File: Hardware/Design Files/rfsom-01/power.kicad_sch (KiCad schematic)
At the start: 26 parts

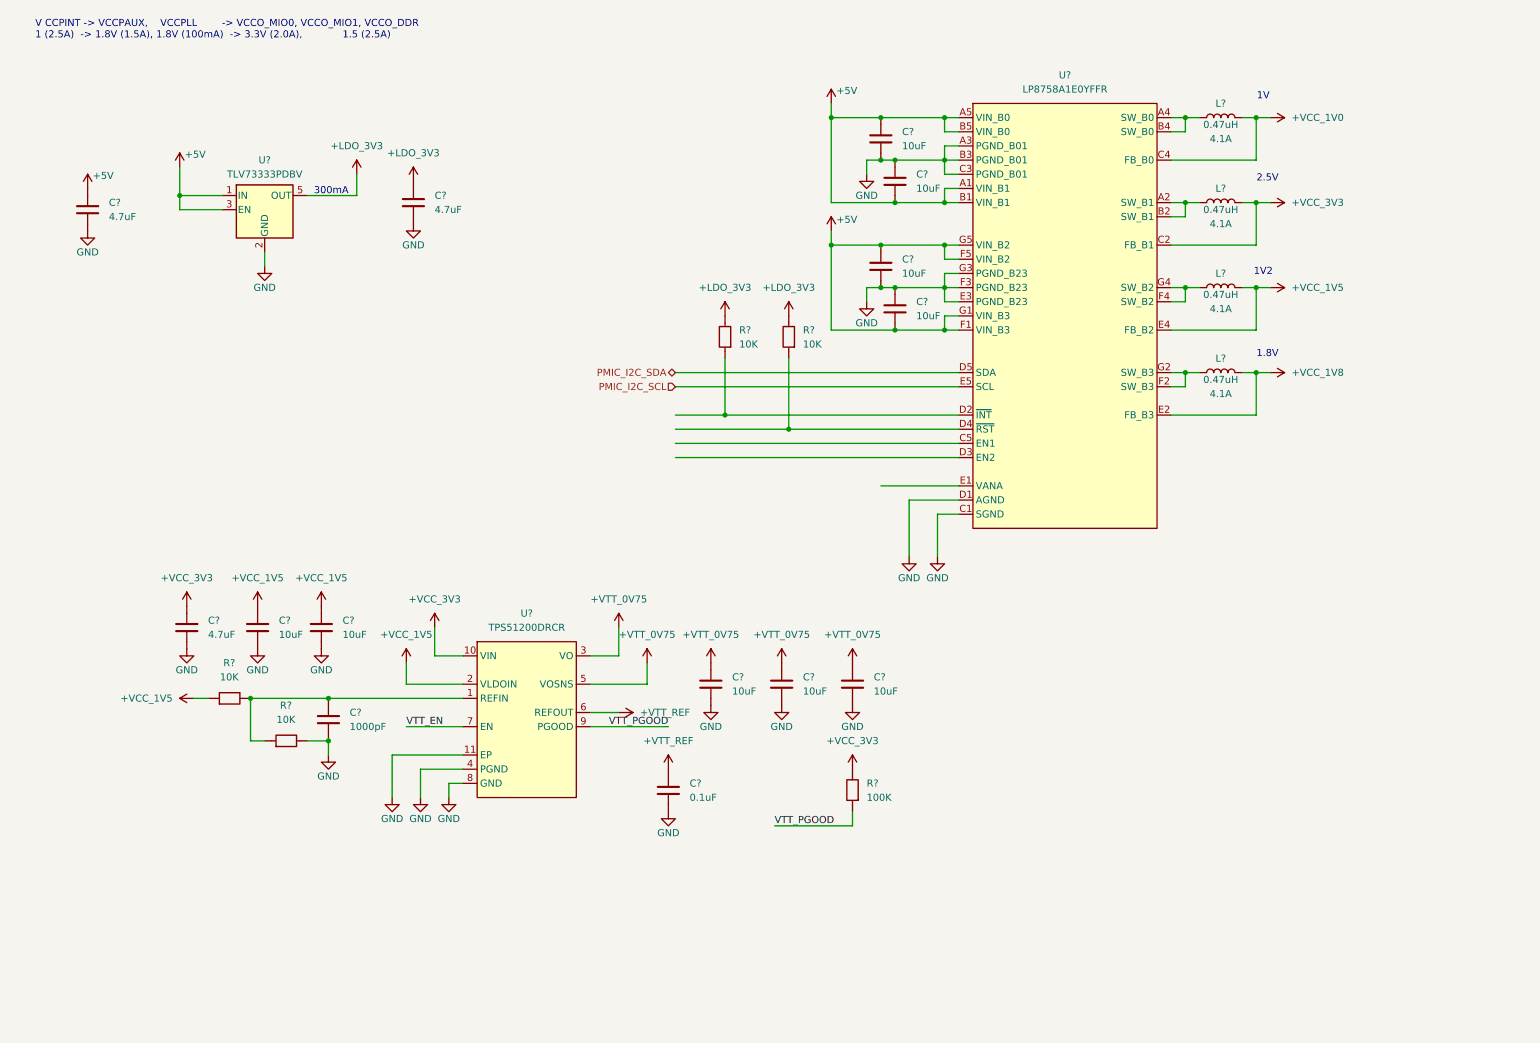
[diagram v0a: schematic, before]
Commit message: ddr progress; added more conns;
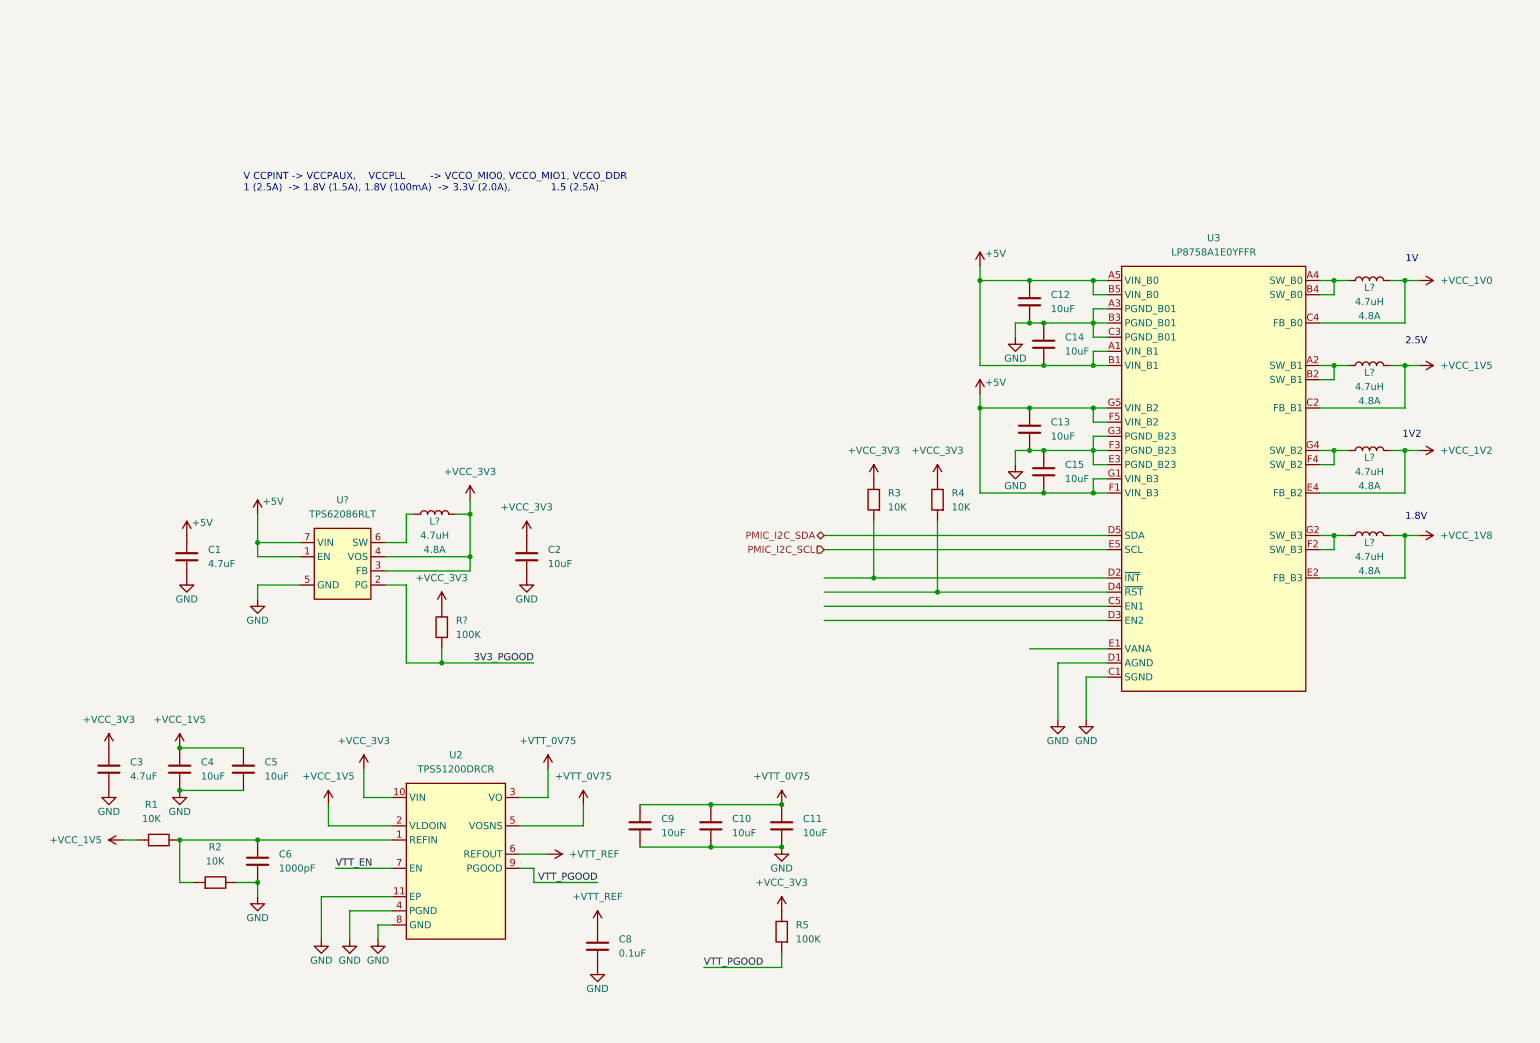
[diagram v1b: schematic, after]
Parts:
- removed C?: CL21B475KAFNNNE, Capacitor_SMD:C_0805_2012Metric_Pad1.18x1.45mm_HandSolder, symbol Capacitors:CL21B475KAFNNNE
- removed L? (x4): MAMK2520HR47M, Inductors:MAMK2520HR47M, symbol Inductors:MAMK2520HR47M
- removed U?: TLV73333PDBV, Package_TO_SOT_SMD:SOT-23-5, symbol Regulator_Linear:TLV73333PDBV
- added C2: GRM188R60G106ME47, Capacitor_SMD:C_0603_1608Metric, symbol Capacitors:GRM188R60G106ME47
- added L? (x5): DFE322512F-R47M=P2, Inductors:IND_1210, symbol Inductors:DFE322512F-R47M=P2
- added R?: RC0402FR-07100KL, Resistor_SMD:R_0402_1005Metric_Pad0.72x0.64mm_HandSolder, symbol Resistors:RC0402FR-07100KL
- added U?: TPS62086RLT, ICs:RLT0007A, symbol ICs:TPS62086RLT
- gave numbers to parts that had none: 20
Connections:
- net +LDO_3V3 is gone; now on net +VCC_3V3: R3.2, R4.2
- net +5V: now also U?.1 (EN), U?.7 (VIN)
- net +VCC_1V0: now also L?.2
- net +VCC_1V5: now also U3.C2 (FB_B1), L?.2; no longer U3.E4 (FB_B2)
- net +VCC_1V8: now also L?.2
- net +VCC_3V3: now also C2.1, L?.2, R?.2, U?.3 (FB), U?.4 (VOS); no longer U3.C2 (FB_B1)
- net GND: now also C2.2, U?.5 (GND)
- net at U3.A4 (SW_B0), U3.B4 (SW_B0): now also L?.1
- net at U3.A2 (SW_B1), U3.B2 (SW_B1): now also L?.1
- net at U3.F2 (SW_B3), U3.G2 (SW_B3): now also L?.1
- net at U3.F4 (SW_B2), U3.G4 (SW_B2): now also L?.1
- new net: L?.1, U?.6 (SW)
- new net +VCC_1V2: L?.2, U3.E4 (FB_B2)
- new net 3V3_PGOOD: R?.1, U?.2 (PG)
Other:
- note removed: "300mA"
- moved on the sheet: C1, C10, C11, C12, C13, C14, C15, C3, C4, C5, C6, C8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

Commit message: ps progress; added ftdi; mezz pinout pedinging;
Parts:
- added R? (x4): RC0603JR-070RL, Resistor_SMD:R_0603_1608Metric_Pad0.98x0.95mm_HandSolder, symbol Resistors:RC0603JR-070RL
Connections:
- net +VCC_1V0: now also R?.2; no longer L?.2, U3.C4 (FB_B0)
- net +VCC_1V2: now also R?.2; no longer L?.2, U3.E4 (FB_B2)
- net +VCC_1V5: now also R?.2; no longer L?.2, U3.C2 (FB_B1)
- net +VCC_1V8: now also R?.2; no longer L?.2, U3.E2 (FB_B3)
- net +5V renamed +VIN_5V0
- new net: L?.2, R?.1, U3.C2 (FB_B1)
- new net: L?.2, R?.1, U3.E2 (FB_B3)
- new net: L?.2, R?.1, U3.C4 (FB_B0)
- new net: L?.2, R?.1, U3.E4 (FB_B2)
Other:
- moved on the sheet: C1, C10, C11, C12, C13, C14, C15, C2, C3, C4, C5, C6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

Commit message: some ddr routing progress; layerstack per pcbway standard options, review reqd; commit prior to ddr split;
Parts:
- C1: footprint Capacitor_SMD:C_0805_2012Metric_Pad1.18x1.45mm_HandSolder -> Capacitor_SMD:C_0805_2012Metric
- C12, C13, C14, C15: footprint Capacitor_SMD:C_1206_3216Metric_Pad1.33x1.80mm_HandSolder -> Capacitor_SMD:C_1206_3216Metric
- C8: footprint Capacitor_SMD:C_0402_1005Metric_Pad0.74x0.62mm_HandSolder -> Capacitor_SMD:C_0402_1005Metric
- R1, R2, R3, R4: footprint Resistor_SMD:R_0603_1608Metric_Pad0.98x0.95mm_HandSolder -> Resistor_SMD:R_0603_1608Metric
- R10, R11, R12, R9: renamed from R?; footprint Resistor_SMD:R_0603_1608Metric_Pad0.98x0.95mm_HandSolder -> Resistor_SMD:R_0603_1608Metric
- R5: footprint Resistor_SMD:R_0402_1005Metric_Pad0.72x0.64mm_HandSolder -> Resistor_SMD:R_0402_1005Metric
- R8: renamed from R?; footprint Resistor_SMD:R_0402_1005Metric_Pad0.72x0.64mm_HandSolder -> Resistor_SMD:R_0402_1005Metric
- gave numbers to parts that had none: 6
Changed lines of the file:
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@@
 		(on_board yes)
 		(dnp no)
-		(property "Reference" "L?"
+		(property "Reference" "L3"
 			(at 213.36 76.2 0)
 			(effects
@@
 			(project "rfsom-01"
 				(path "/5dade83d-850c-4336-8f49-e0e8e6ebca37/8350ef0f-c5e8-4551-b021-24222e56f4d9"
-					(reference "L?")
+					(reference "L3")
 					(unit 1)
 				)
@@
 		(dnp no)
 		(fields_autoplaced yes)
-		(property "Reference" "R?"
+		(property "Reference" "R10"
 			(at 226.06 68.58 90)
 			(effects
@@
 			)
 		)
-		(property "Footprint" "Resistor_SMD:R_0603_1608Metric_Pad0.98x0.95mm_HandSolder"
+		(property "Footprint" "Resistor_SMD:R_0603_1608Metric"
 			(at 219.71 74.93 0)
 			(effects
@@
 			(project "rfsom-01"
 				(path "/5dade83d-850c-4336-8f49-e0e8e6ebca37/8350ef0f-c5e8-4551-b021-24222e56f4d9"
-					(reference "R?")
+					(reference "R10")
 					(unit 1)
 				)
@@
 			)
 		)
-		(property "Footprint" "Capacitor_SMD:C_0402_1005Metric_Pad0.74x0.62mm_HandSolder"
+		(property "Footprint" "Capacitor_SMD:C_0402_1005Metric"
 			(at 111.76 181.61 0)
 			(effects
@@
 		(dnp no)
 		(fields_autoplaced yes)
-		(property "Reference" "U?"
+		(property "Reference" "U1"
 			(at 53.34 68.58 0)
 			(effects
@@
 			(project ""
 				(path "/5dade83d-850c-4336-8f49-e0e8e6ebca37/8350ef0f-c5e8-4551-b021-24222e56f4d9"
-					(reference "U?")
+					(reference "U1")
 					(unit 1)
 				)
@@
 			)
 		)
-		(property "Footprint" "Resistor_SMD:R_0603_1608Metric_Pad0.98x0.95mm_HandSolder"
+		(property "Footprint" "Resistor_SMD:R_0603_1608Metric"
 			(at 135.89 105.41 0)
 			(effects
@@
 			)
 		)
-		(property "Footprint" "Resistor_SMD:R_0402_1005Metric_Pad0.72x0.64mm_HandSolder"
+		(property "Footprint" "Resistor_SMD:R_0402_1005Metric"
 			(at 144.78 191.77 0)
 			(effects
@@
 		(dnp no)
 		(fields_autoplaced yes)
-		(property "Reference" "R?"
+		(property "Reference" "R12"
 			(at 226.06 99.06 90)
 			(effects
@@
 			)
 		)
-		(property "Footprint" "Resistor_SMD:R_0603_1608Metric_Pad0.98x0.95mm_HandSolder"
+		(property "Footprint" "Resistor_SMD:R_0603_1608Metric"
 			(at 219.71 105.41 0)
 			(effects
@@
 			(project "rfsom-01"
 				(path "/5dade83d-850c-4336-8f49-e0e8e6ebca37/8350ef0f-c5e8-4551-b021-24222e56f4d9"
-					(reference "R?")
+					(reference "R12")
 					(unit 1)
 				)
@@
 			)
 		)
-		(property "Footprint" "Capacitor_SMD:C_0805_2012Metric_Pad1.18x1.45mm_HandSolder"
+		(property "Footprint" "Capacitor_SMD:C_0805_2012Metric"
 			(at 25.4 72.39 0)
 			(effects
@@
 			)
 		)
-		(property "Footprint" "Capacitor_SMD:C_1206_3216Metric_Pad1.33x1.80mm_HandSolder"
+		(property "Footprint" "Capacitor_SMD:C_1206_3216Metric"
 			(at 154.94 64.77 0)
 			(effects
@@
 			)
 		)
-		(property "Footprint" "Capacitor_SMD:C_1206_3216Metric_Pad1.33x1.80mm_HandSolder"
+		(property "Footprint" "Capacitor_SMD:C_1206_3216Metric"
 			(at 152.4 80.01 0)
 			(effects
@@
 		(on_board yes)
 		(dnp no)
-		(property "Reference" "L?"
+		(property "Reference" "L2"
 			(at 213.36 60.96 0)
 			(effects
@@
 			(project ""
 				(path "/5dade83d-850c-4336-8f49-e0e8e6ebca37/8350ef0f-c5e8-4551-b021-24222e56f4d9"
-					(reference "L?")
+					(reference "L2")
 					(unit 1)
 				)
@@
 			)
 		)
-		(property "Footprint" "Resistor_SMD:R_0603_1608Metric_Pad0.98x0.95mm_HandSolder"
+		(property "Footprint" "Resistor_SMD:R_0603_1608Metric"
 			(at 26.67 168.91 0)
 			(effects
@@
 		(dnp no)
 		(fields_autoplaced yes)
-		(property "Reference" "R?"
+		(property "Reference" "R9"
 			(at 226.06 53.34 90)
 			(effects
@@
 			)
 		)
-		(property "Footprint" "Resistor_SMD:R_0603_1608Metric_Pad0.98x0.95mm_HandSolder"
+		(property "Footprint" "Resistor_SMD:R_0603_1608Metric"
 			(at 219.71 59.69 0)
 			(effects
@@
 			(project ""
 				(path "/5dade83d-850c-4336-8f49-e0e8e6ebca37/8350ef0f-c5e8-4551-b021-24222e56f4d9"
-					(reference "R?")
+					(reference "R9")
 					(unit 1)
 				)
@@
 			)
 		)
-		(property "Footprint" "Resistor_SMD:R_0603_1608Metric_Pad0.98x0.95mm_HandSolder"
+		(property "Footprint" "Resistor_SMD:R_0603_1608Metric"
 			(at 36.83 176.53 0)
 			(effects
@@
 		(on_board yes)
 		(dnp no)
-		(property "Reference" "L?"
+		(property "Reference" "L5"
 			(at 213.36 106.68 0)
 			(effects
@@
 			(project "rfsom-01"
 				(path "/5dade83d-850c-4336-8f49-e0e8e6ebca37/8350ef0f-c5e8-4551-b021-24222e56f4d9"
-					(reference "L?")
+					(reference "L5")
 					(unit 1)
 				)
@@
 		(on_board yes)
 		(dnp no)
-		(property "Reference" "L?"
+		(property "Reference" "L1"
 			(at 69.85 72.39 0)
 			(effects
@@
 			(project "rfsom-01"
 				(path "/5dade83d-850c-4336-8f49-e0e8e6ebca37/8350ef0f-c5e8-4551-b021-24222e56f4d9"
-					(reference "L?")
+					(reference "L1")
 					(unit 1)
 				)
@@
 			)
 		)
-		(property "Footprint" "Capacitor_SMD:C_1206_3216Metric_Pad1.33x1.80mm_HandSolder"
+		(property "Footprint" "Capacitor_SMD:C_1206_3216Metric"
 			(at 154.94 87.63 0)
 			(effects
@@
 		(dnp no)
 		(fields_autoplaced yes)
-		(property "Reference" "R?"
+		(property "Reference" "R11"
 			(at 226.06 83.82 90)
 			(effects
@@
 			)
 		)
-		(property "Footprint" "Resistor_SMD:R_0603_1608Metric_Pad0.98x0.95mm_HandSolder"
+		(property "Footprint" "Resistor_SMD:R_0603_1608Metric"
 			(at 219.71 90.17 0)
 			(effects
@@
 			(project "rfsom-01"
 				(path "/5dade83d-850c-4336-8f49-e0e8e6ebca37/8350ef0f-c5e8-4551-b021-24222e56f4d9"
-					(reference "R?")
+					(reference "R11")
 					(unit 1)
 				)
@@
 			)
 		)
-		(property "Footprint" "Resistor_SMD:R_0603_1608Metric_Pad0.98x0.95mm_HandSolder"
+		(property "Footprint" "Resistor_SMD:R_0603_1608Metric"
 			(at 124.46 105.41 0)
 			(effects
@@
 		(on_board yes)
 		(dnp no)
-		(property "Reference" "L?"
+		(property "Reference" "L4"
 			(at 213.36 91.44 0)
 			(effects
@@
 			(project "rfsom-01"
 				(path "/5dade83d-850c-4336-8f49-e0e8e6ebca37/8350ef0f-c5e8-4551-b021-24222e56f4d9"
-					(reference "L?")
+					(reference "L4")
 					(unit 1)
 				)
@@
 		(dnp no)
 		(fields_autoplaced yes)
-		(property "Reference" "R?"
+		(property "Reference" "R8"
 			(at 73.66 90.1699 0)
 			(effects
@@
 			)
 		)
-		(property "Footprint" "Resistor_SMD:R_0402_1005Metric_Pad0.72x0.64mm_HandSolder"
+		(property "Footprint" "Resistor_SMD:R_0402_1005Metric"
 			(at 71.12 97.79 0)
 			(effects
@@
 			(project "rfsom-01"
 				(path "/5dade83d-850c-4336-8f49-e0e8e6ebca37/8350ef0f-c5e8-4551-b021-24222e56f4d9"
-					(reference "R?")
+					(reference "R8")
 					(unit 1)
 				)
@@
 			)
 		)
-		(property "Footprint" "Capacitor_SMD:C_1206_3216Metric_Pad1.33x1.80mm_HandSolder"
+		(property "Footprint" "Capacitor_SMD:C_1206_3216Metric"
 			(at 152.4 57.15 0)
 			(effects

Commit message: added starage, usb sch; more design progress in sch;
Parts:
- added C186: CL21B475KPFNNNE, Capacitor_SMD:C_0805_2012Metric, symbol Capacitors:CL21B475KPFNNNE
- added C187: CL05B102KB5NNNC, Capacitor_SMD:C_0402_1005Metric, symbol Capacitors:CL05B102KB5NNNC
- added C188, C189, C191, C192, C193: CL21B106KQQNFNE, Capacitor_SMD:C_0805_2012Metric, symbol Capacitors:CL21B106KQQNFNE
- added C190: CL05B104KA5NNNC, Capacitor_SMD:C_0402_1005Metric, symbol Capacitors:CL05B104KA5NNNC
- added R124, R125: RC0603FR-0710KL, Resistor_SMD:R_0603_1608Metric, symbol Resistors:RC0603FR-0710KL
- added R126: RC0402FR-07100KL, Resistor_SMD:R_0402_1005Metric, symbol Resistors:RC0402FR-07100KL
- added U12: TPS51200DRCR, Package_SON:VSON-10-1EP_3x3mm_P0.5mm_EP1.65x2.4mm, symbol ICs:TPS51200DRCR
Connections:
- net +VCC_3V3: now also C186.1, R126.2, U12.10 (VIN)
- net GND: now also C186.2, C187.2, C188.2, C189.2, C190.2, C191.2, C192.2, C193.2, R125.2, U12.11 (EP), U12.4 (PGND), U12.8 (GND)
- net +VCC_1V5 renamed +PS_VCC_1V5
- net +VTT_0V75 renamed +PS_VTT_0V75
- net +VTT_REF renamed +PS_VTT_REF
- net +PS_VTT_REF: now also U12.6 (REFOUT)
- net VTT_EN renamed PS_VTT_EN
- net VTT_PGOOD renamed PS_VTT_PGOOD
- new net: C187.1, R124.2, R125.1, U12.1 (REFIN)
- new net +PL_VCC_1V5: C188.1, C189.1, R124.1, U12.2 (VLDOIN)
- new net +PL_VTT_0V75: C191.1, C192.1, C193.1, U12.3 (VO), U12.5 (VOSNS)
- new net +PL_VTT_REF: C190.1
- new net PL_VTT_EN: U12.7 (EN)
- new net PL_VTT_PGOOD: R126.1, U12.9 (PGOOD)
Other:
- note added: "3A OUT"
- note added: "4A OUT"
- moved on the sheet: C1, C10, C11, C12, C13, C14, C15, C2, C3, C4, C5, C6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
